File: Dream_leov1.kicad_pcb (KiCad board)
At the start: 2 copper layers, 95.1 x 80 mm, 36 parts, among them IC1 TGS2611-C00, J1 GPIO, J11 10132328-10011LF, J2 Qwiic_Vertical, J3 679305124022, J4 Qwiic_Vertical, J5 M20-7830542, J6 Qwiic_Vertical, J7 5013310607, J8 Qwiic_4pin_Vertical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

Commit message: update silkscreen
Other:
- board text added: "- - - - -"
- board text added: "3.3V"
- board text added: "5V"
- board text added: "I2C 1"
- board text added: "I2C 3"
- board text added: "I2C 4"
- board text added: "I2C 5"
- board text added: "SPI"
- board text added: "UART"
- board text removed: "3 v"
- board text removed: "5 v"
- board text removed: "i2c bus 1"
- board text removed: "i2c bus 3"
- board text removed: "i2c bus 4"
- board text removed: "i2c bus 5"
- board text removed: "spi hdr"
- board text removed: "uart"

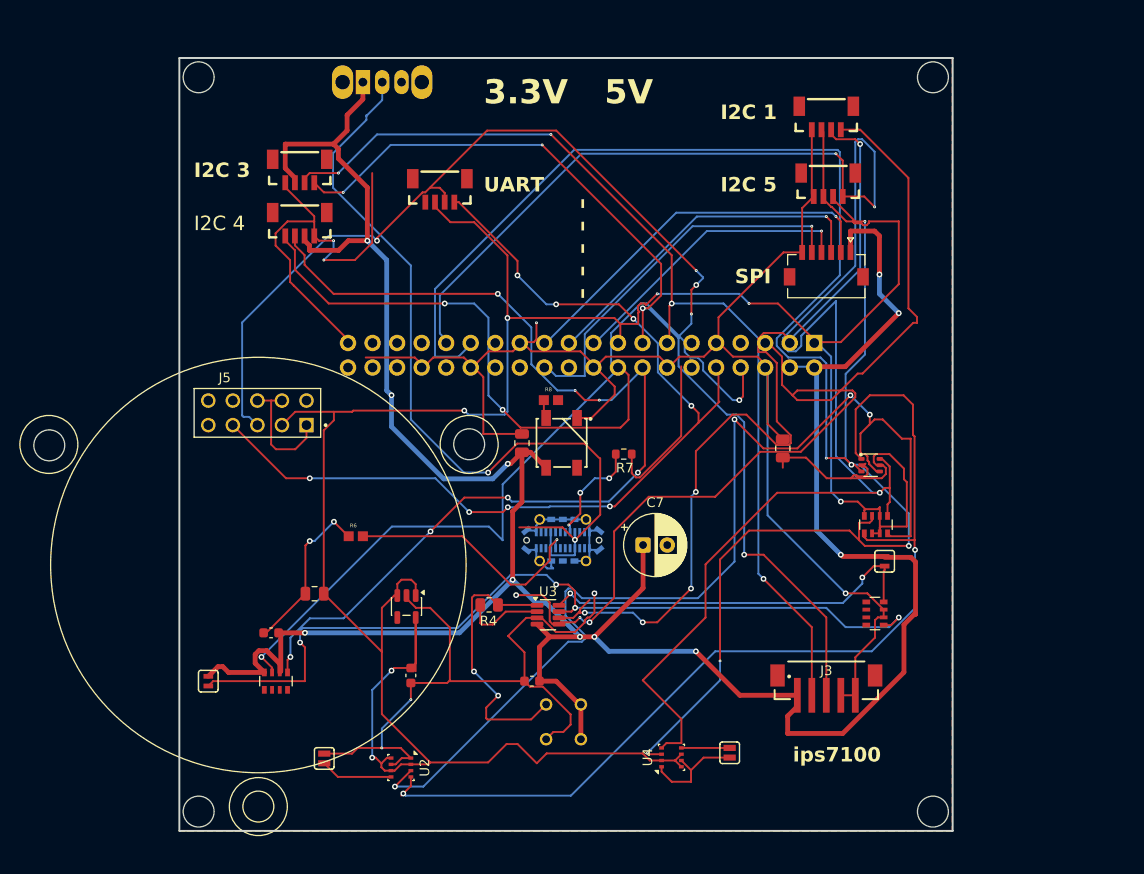
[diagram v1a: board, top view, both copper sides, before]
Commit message: Add files via upload
finishing touches on edge cut and errors
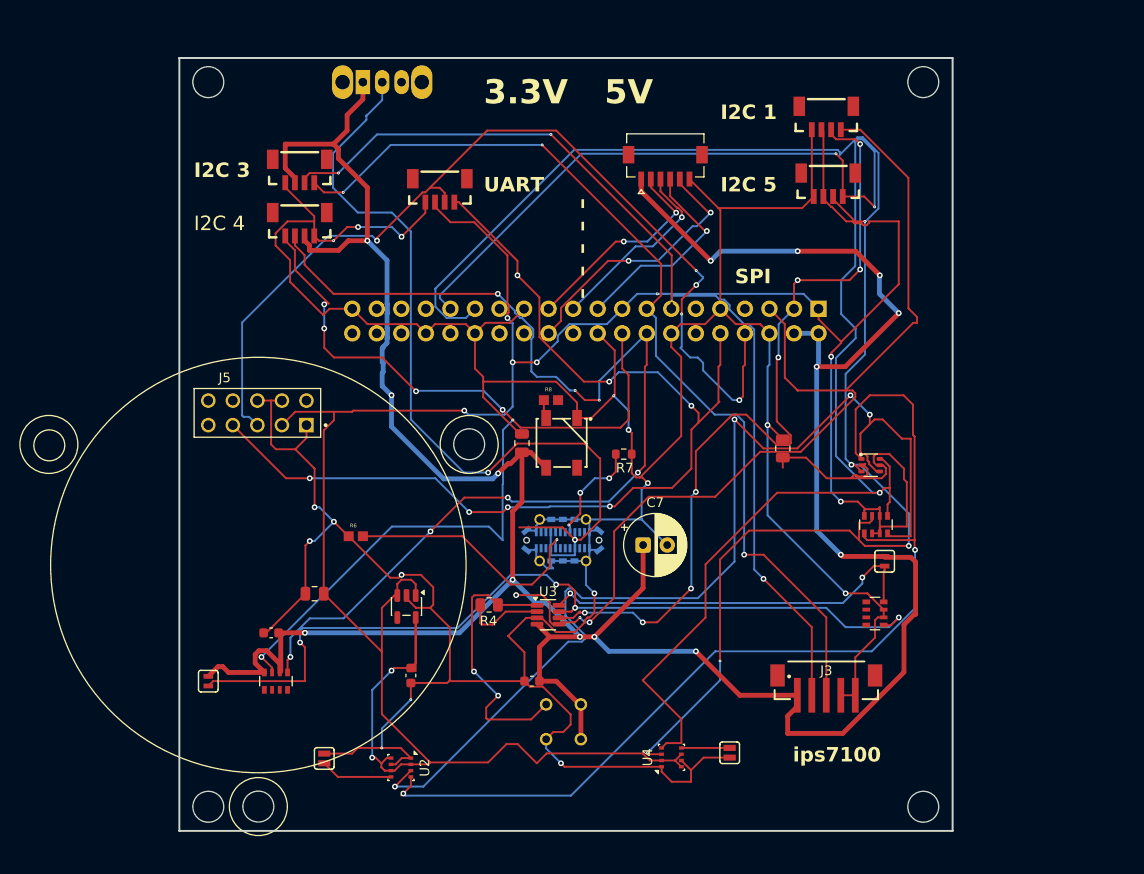
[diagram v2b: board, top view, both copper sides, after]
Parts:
- moved J7 20.6 mm to (102.8, 29.3), turned to 180 degrees
- moved J1 3.57 mm to (118.7, 45.0)
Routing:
- net GND: track 342.3 -> 407.9 mm, vias 9 -> 16
- net /GPIO5/SDA5: track 193.8 -> 161.2 mm, vias 6 -> 5
- net +5V: track 283.6 -> 308.8 mm, vias 11 -> 14
- net /GPIO11/SPI0.SCLK: track 39.6 -> 21.9 mm, vias 1 -> 2
- net /GPIO6/SCL5: track 178.0 -> 160.4 mm
- net /GPIO9/SPI0.MISO: track 35.7 -> 20.1 mm
- net /GPIO8/SPI0.CE0: track 39.5 -> 27.7 mm, vias 1 -> 2
- net /GPIO14/TXD0: track 111.5 -> 101.4 mm
- net /GPIO10/SPI0.MOSI: track 30.3 -> 21.7 mm
- net /GPIO24/SCL4: track 111.8 -> 104.0 mm, vias 3 -> 6
- net /GPIO15/RXD0: track 100.4 -> 107.7 mm, vias 8 -> 7
- net /GPIO23/SDA4: track 106.5 -> 113.5 mm
- net /GPIO3/SCL1: track 106.1 -> 102.4 mm
- net /GPIO2/SDA1: track 87.9 -> 84.9 mm, vias 5 -> 8
- net /GPIO27/SDA3: track 103.8 -> 101.4 mm
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- removed copper zone on F.Cu, net GND
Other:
- board size 95.1 x 80 mm -> 80 x 80 mm

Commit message: Add files via upload
methane sens flipped and clutter cleaned by gpio3 and  90s cleaned, copper zone added on f.cu and DRC ran and checked. spi logo moved. all the lose traces I could find I cut.
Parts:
- moved C3 2.63 mm to (116.0, 57.0)
- moved C5 2.50 mm to (89.0, 81.0)
- moved IC1 0.09 mm to (90.5, 89.6)
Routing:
- net /GPIO3/SCL1: track 102.4 -> 90.0 mm, vias 3 -> 2
- net /GPIO2/SDA1: track 84.9 -> 76.8 mm
- net /BME_SDA: track 112.1 -> 104.3 mm
- net /5V_BUS_USB: track 89.8 -> 83.5 mm
- net +3V3: track 295.4 -> 289.3 mm
- net /GPIO14/TXD0: track 101.4 -> 96.1 mm, vias 5 -> 3
- net /GPIO6/SCL5: track 160.4 -> 156.2 mm
- net +5V: track 308.8 -> 307.0 mm
- net /BME_SCL: track 102.6 -> 103.6 mm
- net GND: track 407.9 -> 408.8 mm, vias 16 -> 14
- added copper zone on F.Cu, net GND

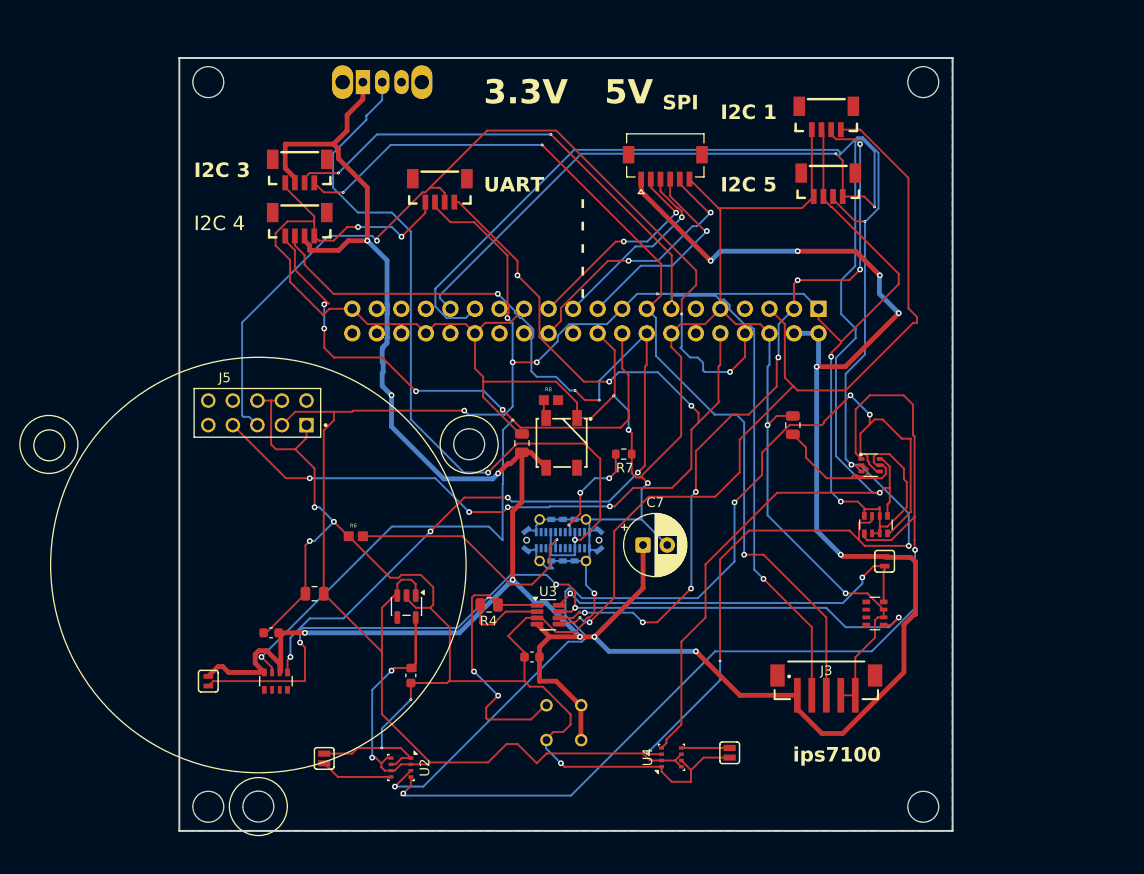
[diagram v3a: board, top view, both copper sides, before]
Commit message: partially fixed leo board
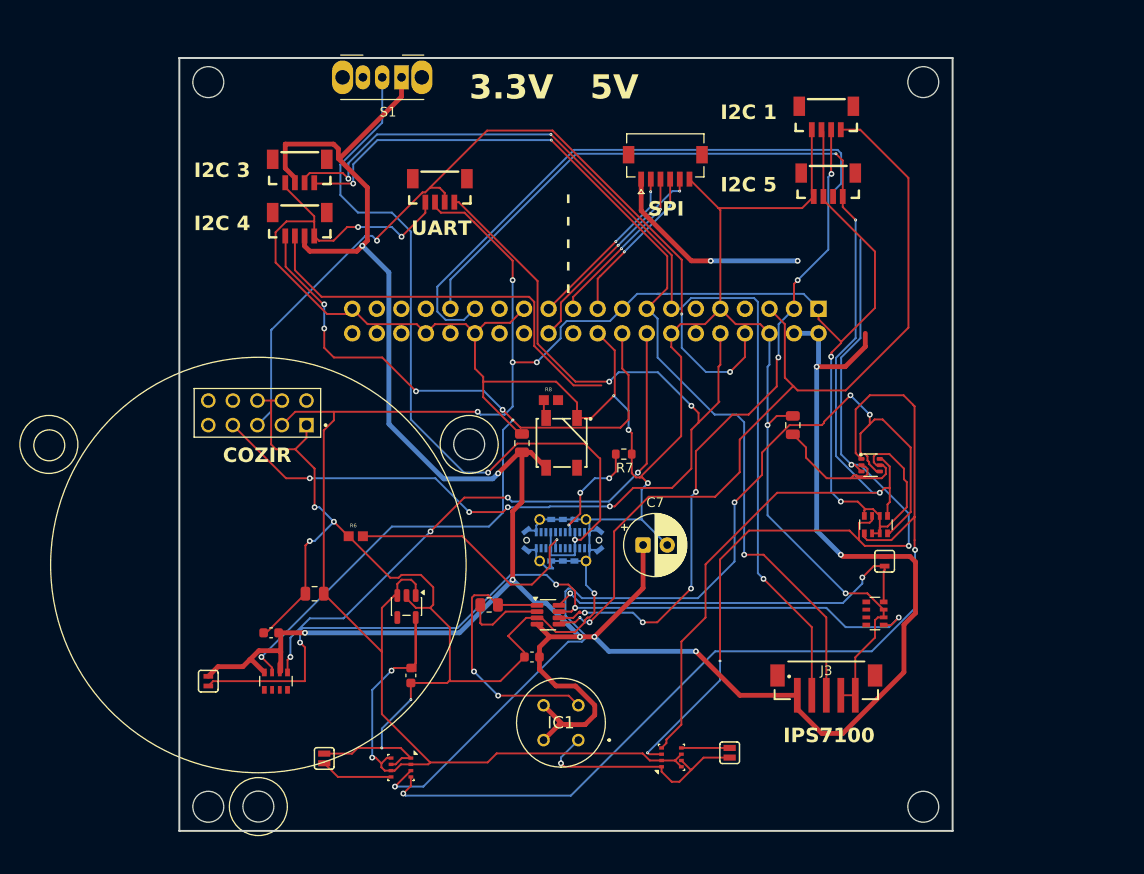
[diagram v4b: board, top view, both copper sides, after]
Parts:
- IC1, S1: moved to F.Cu
- U3: value INA219BxDCN -> INA219
- moved S1 4.03 mm to (75.5, 21.0), turned to 180 degrees
- moved IC1 3.30 mm to (93.8, 89.6), turned to 0 degrees
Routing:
- net /GPIO6/SCL5: track 156.2 -> 137.2 mm
- net GND: track 408.8 -> 395.0 mm
- net /GPIO5/SDA5: track 161.2 -> 147.4 mm, vias 5 -> 4
- net /GPIO23/SDA4: track 113.5 -> 104.8 mm, vias 7 -> 4
- net +5V: track 307.0 -> 299.4 mm, vias 14 -> 11
- net /GPIO2/SDA1: track 76.8 -> 70.5 mm, vias 8 -> 7
- net /GPIO14/TXD0: track 96.1 -> 90.2 mm
- net /GPIO8/SPI0.CE0: track 27.7 -> 22.5 mm
- net /GPIO10/SPI0.MOSI: track 21.7 -> 16.5 mm, vias 1 -> 2
- net /GPIO11/SPI0.SCLK: track 21.9 -> 17.8 mm
- net +3V3: track 289.3 -> 285.3 mm, vias 9 -> 8
- net /GPIO24/SCL4: track 104.0 -> 100.7 mm
- net /GPIO9/SPI0.MISO: track 20.1 -> 17.2 mm, vias 1 -> 2
- net /GPIO27/SDA3: track 101.4 -> 104.1 mm, vias 4 -> 3
- net /GPIO22/SCL3: track 100.1 -> 102.4 mm
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- removed copper zone on F.Cu, net GND
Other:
- board text added: "COZIR"
- board text added: "IPS7100"
- board text removed: "ips7100"

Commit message: restarted traces
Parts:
- removed J8: Qwiic_4pin_Vertical, SparkFun-Connector:JST_1x04_P1.0mm_Vertical_SMD
- added J4: Qwiic_Vertical, SparkFun-Connector:JST_1x04_P1.0mm_Vertical_SMD, F.Cu at (68.0, 36.0)
- moved S1 43.5 mm to (119.0, 21.0)
- moved J6 27.5 mm to (107.0, 32.0)
- moved J7 22.5 mm to (80.5, 32.0)
- moved j9 5.29 mm to (118.0, 30.0)
- moved J2 4.49 mm to (118.0, 36.0)
- moved J4 3.06 mm to (68.0, 30.0)
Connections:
- J2 pad 3: /GPIO5/SDA5 -> /GPIO2/SDA1
- j9 pad 3: /GPIO2/SDA1 -> /GPIO23/SDA4
- j9 pad 4: /GPIO3/SCL1 -> /GPIO24/SCL4
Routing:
- net GND: track 395.0 -> 75.3 mm, vias 14 -> 3
- net +3V3: track 285.3 -> 33.7 mm, vias 8 -> 2
- net +5V: track 299.4 -> 100.5 mm, vias 11 -> 0
- net /GPIO5/SDA5: track 147.4 -> 18.6 mm, vias 4 -> 1
- net /GPIO6/SCL5: track 137.2 -> 16.4 mm, vias 3 -> 1
- net /GPIO15/RXD0: track 108.3 -> 0.00 mm, vias 6 -> 0
- net /BME_SDA: track 103.8 -> 0.00 mm, vias 4 -> 0
- net /BME_SCL: track 103.3 -> 0.00 mm, vias 2 -> 0
- net /GPIO14/TXD0: track 90.2 -> 0.00 mm, vias 3 -> 0
- net /INA_ADD0: track 87.4 -> 0.00 mm, vias 4 -> 0
- net /5V_BUS_USB: track 82.8 -> 0.00 mm, vias 2 -> 0
- net /GPIO23/SDA4: track 104.8 -> 30.5 mm, vias 4 -> 1
- net /GPIO3/SCL1: track 89.1 -> 16.7 mm, vias 2 -> 1
- net /GPIO24/SCL4: track 100.7 -> 33.5 mm, vias 6 -> 1
- net /GPIO22/SCL3: track 102.4 -> 38.7 mm, vias 3 -> 1
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
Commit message: halfway done v3
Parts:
- U3: value INA219 -> INA219BxDCN
- moved JP3 40.5 mm to (85.0, 72.5), turned to 180 degrees
- moved R2 40.0 mm to (84.5, 78.5)
- moved JP2 30.7 mm to (85.0, 75.0), turned to 180 degrees
- moved Q1 28.9 mm to (99.5, 76.5)
- moved R1 28.6 mm to (99.5, 81.0), turned to 0 degrees
- moved C4 28.2 mm to (115.0, 51.0), turned to 180 degrees
- moved C3 18.2 mm to (99.0, 50.5), turned to 0 degrees
- moved J3 14.6 mm to (113.0, 96.5), turned to 180 degrees
- moved JP1 10.9 mm to (78.0, 88.5)
- moved R7 10.6 mm to (88.0, 58.5), turned to -90 degrees
- moved U2 8.31 mm to (82.5, 88.0)
- moved R8 8.09 mm to (99.0, 53.5)
- moved R4 6.88 mm to (89.4, 80.5)
- moved C5 6.67 mm to (82.5, 82.5), turned to 0 degrees
- moved C1 6.24 mm to (82.5, 84.5), turned to 0 degrees
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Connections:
- C1 pad 1: +3V3 -> +3.3V
- C2 pad 1: +3V3 -> +3.3V
- C3 pad 1: +3V3 -> +3.3V
- J1 pad 17: +3V3 -> +3.3V
- J2 pad : /GPIO3/SCL1 -> (no net)
- J2 pad 2: +3V3 -> +3.3V
- J2 pad 3: /GPIO2/SDA1 -> /GPIO5/SDA5
- J6 pad 2: +3V3 -> +3.3V
- Q1 pad 2: +3V3 -> +3.3V
- Q1 pad 5: +3V3 -> +3.3V
- R1 pad 2: +3V3 -> +3.3V
- R1 pad 4: +3V3 -> +3.3V
- R1 pad 6: +3V3 -> +3.3V
- R1 pad 7: +3V3 -> +3.3V
- R8 pad 2: unconnected-(R8-Pad2) -> /GPIO18/PCM.CLK
- U1 pad 1: +3V3 -> +3.3V
- U1 pad 5: +3V3 -> +3.3V
- U1 pad ee: +3V3 -> (no net)
- U2 pad 2: +3V3 -> +3.3V
- U2 pad 6: +3V3 -> +3.3V
- U2 pad 8: +3V3 -> +3.3V
- U4 pad 2: +3V3 -> +3.3V
- U4 pad 6: +3V3 -> +3.3V
- U4 pad 8: +3V3 -> +3.3V
- j9 pad 2: +3V3 -> +3.3V
- j9 pad 3: /GPIO23/SDA4 -> /GPIO2/SDA1
- j9 pad 4: /GPIO24/SCL4 -> /GPIO3/SCL1
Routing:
- net GND: track 75.3 -> 212.3 mm, vias 3 -> 6
- net +3.3V: track 0.00 -> 124.6 mm, vias 0 -> 7
- net +5V: track 100.5 -> 213.0 mm, vias 0 -> 1
- net /5V_BUS_USB: track 0.00 -> 75.1 mm, vias 0 -> 4
- net +3V3: track 33.7 -> 0.00 mm, vias 2 -> 0
- net /BME_SCL: track 0.00 -> 33.1 mm, vias 0 -> 2
- net /BME_SDA: track 0.00 -> 24.5 mm, vias 0 -> 2
- net /INA+: track 0.00 -> 12.9 mm, vias 0 -> 1
- net /GPIO5/SDA5: track 18.6 -> 31.3 mm
- net Net-(J11-CC1): track 0.00 -> 12.2 mm, vias 0 -> 1
- net /GPIO6/SCL5: track 16.4 -> 28.3 mm
- net Net-(D1-DIN): track 0.00 -> 10.8 mm
- net /INA_ADD0: track 0.00 -> 9.77 mm
- net /GPIO18/PCM.CLK: track 0.00 -> 8.71 mm
- net /INA_ADD1: track 0.00 -> 5.67 mm
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
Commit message: almost done; need to clean up bottom half maybe
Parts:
- C3, C4: moved to B.Cu
- moved R6 21.0 mm to (86.0, 54.0), turned to -90 degrees
- moved R5 15.9 mm to (80.1, 76.7), turned to 0 degrees
- moved C6 14.6 mm to (75.5, 73.0)
- moved C2 8.97 mm to (75.5, 75.0), turned to 0 degrees
- moved U1 4.81 mm to (78.5, 84.0)
- moved R7 4.53 mm to (88.5, 54.0)
- moved C3 2.50 mm to (99.0, 53.0)
- moved C4 2.50 mm to (115.0, 53.5)
- moved R8 2.50 mm to (99.0, 56.0)
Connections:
- J2 pad : (no net) -> /GPIO3/SCL1
- J2 pad 3: /GPIO5/SDA5 -> /GPIO2/SDA1
- J5 pad 3: +3V3 -> +3.3V
- j9 pad 3: /GPIO2/SDA1 -> /GPIO23/SDA4
- j9 pad 4: /GPIO3/SCL1 -> /GPIO24/SCL4
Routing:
- net /GPIO14/TXD0: track 0.00 -> 76.7 mm, vias 0 -> 3
- net /GPIO15/RXD0: track 0.00 -> 76.6 mm, vias 0 -> 3
- net +3.3V: track 124.6 -> 194.3 mm, vias 7 -> 8
- net /GPIO22/SCL3: track 38.7 -> 98.2 mm, vias 1 -> 3
- net /GPIO27/SDA3: track 41.4 -> 99.2 mm, vias 1 -> 3
- net GND: track 212.3 -> 261.5 mm
- net /GPIO6/SCL5: track 28.3 -> 74.0 mm, vias 1 -> 4
- net +5V: track 213.0 -> 258.0 mm, vias 1 -> 5
- net /GPIO5/SDA5: track 31.3 -> 75.7 mm, vias 1 -> 4
- net Net-(J11-CC2): track 0.00 -> 17.3 mm, vias 0 -> 1
- net Net-(J11-CC1): track 12.2 -> 16.5 mm
- net /5V_BUS_USB: track 75.1 -> 78.3 mm
- net /GPIO18/PCM.CLK: track 8.71 -> 11.1 mm
- net Net-(D1-DIN): track 10.8 -> 9.35 mm
- added copper zone on B.Cu, net GND

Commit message: fixed issues; update schematic
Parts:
- added R11: 3.3k, Resistor_SMD:R_0402_1005Metric, F.Cu at (111.0, 74.0)
- added R12: 3.3k, Resistor_SMD:R_0402_1005Metric, F.Cu at (111.0, 76.0)
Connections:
- C1 pad 1: +3.3V -> BME_3V3
- C3 pad 1: +3.3V -> BME_3V3
- J1 pad : +3.3V -> (no net)
- J2 pad : /GPIO3/SCL1 -> (no net)
- J2 pad 3: /GPIO2/SDA1 -> /GPIO5/SDA5
- Q1 pad 2: +3.3V -> BME_3V3
- Q1 pad 5: +3.3V -> BME_3V3
- R1 pad 6: +3.3V -> BME_3V3
- R1 pad 7: +3.3V -> BME_3V3
- U1 pad 5: +3.3V -> BME_3V3
- U1 pad en: +3.3V -> (no net)
- U2 pad 2: +3.3V -> BME_3V3
- U2 pad 6: +3.3V -> BME_3V3
- U2 pad 8: +3.3V -> BME_3V3
- j9 pad 3: /GPIO23/SDA4 -> /GPIO2/SDA1
- j9 pad 4: /GPIO24/SCL4 -> /GPIO3/SCL1
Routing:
- net BME_3V3: track 0.00 -> 6.27 mm
- net +3.3V: track 194.3 -> 188.0 mm
